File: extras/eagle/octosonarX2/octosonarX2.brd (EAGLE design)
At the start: 68.6 x 45.7 mm, 47 parts, among them IC1 74HC125D, IC2 74HC125D, IC3 74HC125D, IC4 74HC125D, IC5 PCF8575C

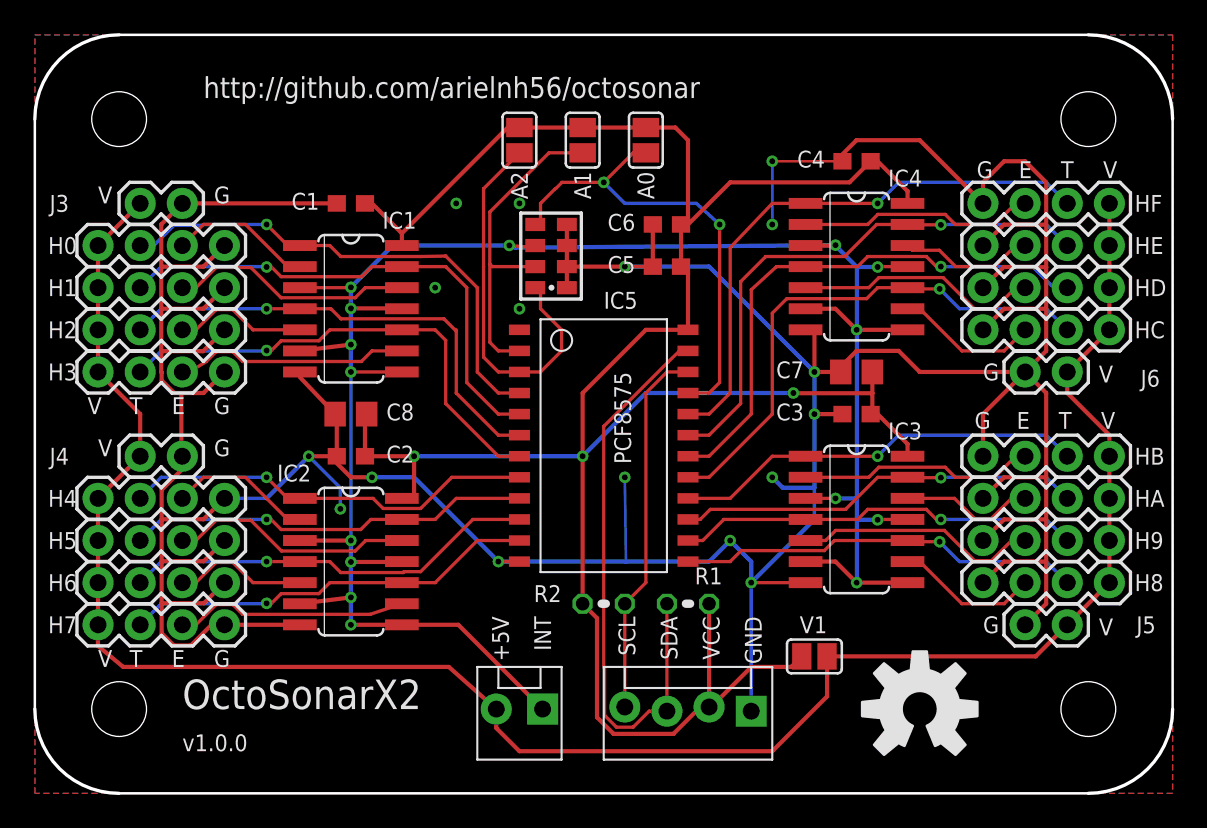
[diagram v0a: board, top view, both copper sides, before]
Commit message: Update octosonarX2.brd to 1.0.1
Moved the 5V line away from the screw hole by moving it to bottom layer. This never caused any reported problem, but I was worried about it and was supplying a plastic screw with each unit just in case. This error was introduced between v0 and V1 when I re-did all the power lines at 10mil.
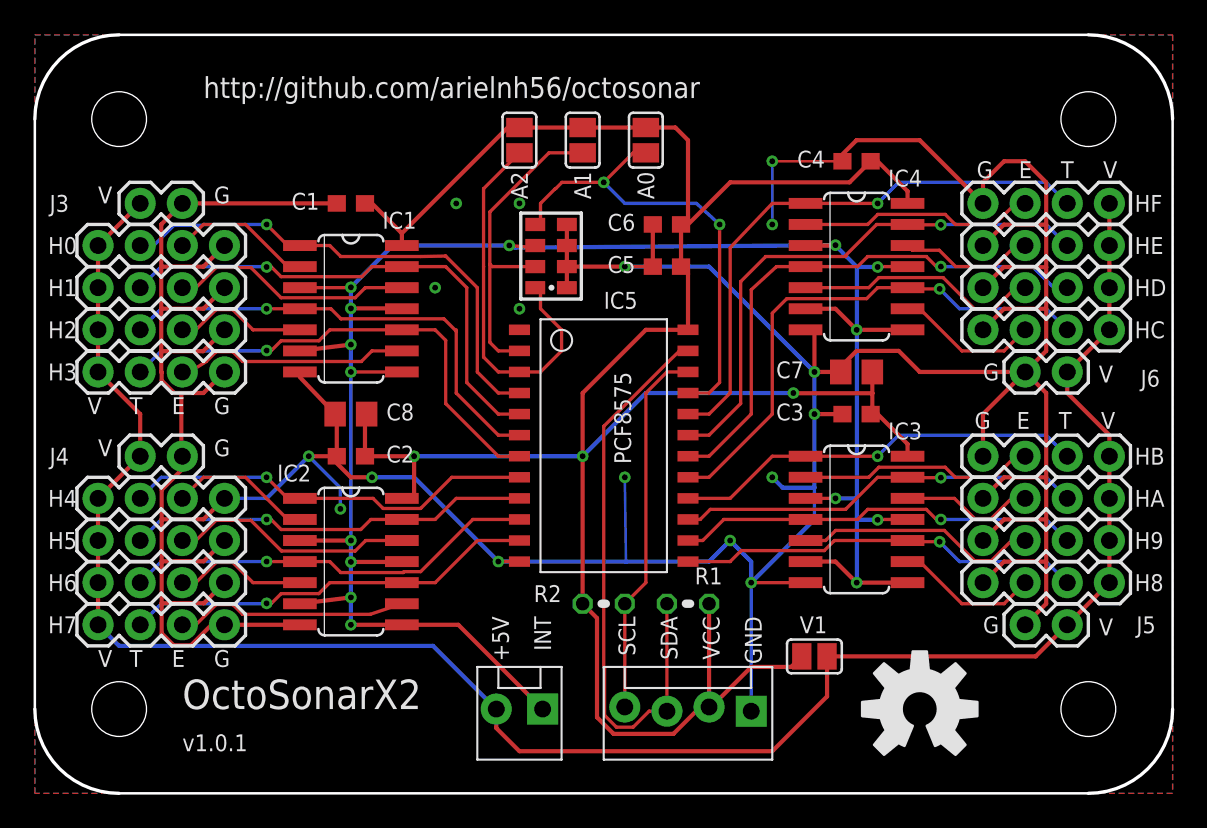
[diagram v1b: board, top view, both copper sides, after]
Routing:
- net +5V: track 124.7 -> 123.9 mm
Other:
- board text added: "v1.0.1"
- board text removed: "v1.0.0"
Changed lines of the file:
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@@
 <?xml version="1.0" encoding="utf-8"?>
 <!DOCTYPE eagle SYSTEM "eagle.dtd">
-<eagle version="8.2.2">
+<eagle version="9.2.2">
 <drawing>
 <settings>
 <setting alwaysvectorfont="no"/>
+<setting keepoldvectorfont="yes"/>
 <setting verticaltext="up"/>
 </settings>
@@
 <layer number="21" name="tPlace" color="7" fill="1" visible="yes" active="yes"/>
 <layer number="22" name="bPlace" color="7" fill="1" visible="no" active="yes"/>
-<layer number="23" name="tOrigins" color="15" fill="1" visible="no" active="yes"/>
+<layer number="23" name="tOrigins" color="15" fill="1" visible="yes" active="yes"/>
 <layer number="24" name="bOrigins" color="15" fill="1" visible="no" active="yes"/>
 <layer number="25" name="tNames" color="7" fill="1" visible="yes" active="yes"/>
@@
 <layer number="37" name="tTest" color="7" fill="1" visible="no" active="yes"/>
 <layer number="38" name="bTest" color="7" fill="1" visible="no" active="yes"/>
-<layer number="39" name="tKeepout" color="4" fill="11" visible="no" active="yes"/>
+<layer number="39" name="tKeepout" color="4" fill="11" visible="yes" active="yes"/>
 <layer number="40" name="bKeepout" color="1" fill="11" visible="no" active="yes"/>
-<layer number="41" name="tRestrict" color="4" fill="10" visible="no" active="yes"/>
+<layer number="41" name="tRestrict" color="4" fill="10" visible="yes" active="yes"/>
 <layer number="42" name="bRestrict" color="1" fill="10" visible="no" active="yes"/>
 <layer number="43" name="vRestrict" color="2" fill="10" visible="no" active="yes"/>
@@
 <layer number="49" name="Reference" color="7" fill="1" visible="no" active="yes"/>
 <layer number="50" name="dxf" color="7" fill="1" visible="no" active="no"/>
-<layer number="51" name="tDocu" color="7" fill="1" visible="no" active="yes"/>
+<layer number="51" name="tDocu" color="7" fill="1" visible="yes" active="yes"/>
 <layer number="52" name="bDocu" color="7" fill="1" visible="no" active="yes"/>
 <layer number="53" name="tGND_GNDA" color="7" fill="9" visible="no" active="no"/>
@@
 <text x="8.89" y="5.08" size="1.778" layer="21" font="vector" ratio="15">OctoSonarX2</text>
 <text x="10.16" y="41.91" size="1.27" layer="21" font="vector" ratio="15">http://github.com/arielnh56/octosonar</text>
-<text x="8.89" y="2.54" size="1.016" layer="21" font="vector" ratio="15">v1.0.0</text>
+<text x="8.89" y="2.54" size="1.016" layer="21" font="vector" ratio="15">v1.0.1</text>
 <text x="64.389" y="37.084" size="1.016" layer="21" font="vector" ratio="15">V</text>
 <text x="3.81" y="20.32" size="1.016" layer="21" font="vector" ratio="15">V</text>
@@
 <param name="dpMaxLengthDifference" value="10mm"/>
 <param name="dpGapFactor" value="2.5"/>
-<param name="checkGrid" value="0"/>
 <param name="checkAngle" value="0"/>
 <param name="checkFont" value="1"/>
 <param name="checkRestrict" value="1"/>
+<param name="checkStop" value="0"/>
+<param name="checkValues" value="0"/>
+<param name="checkNames" value="1"/>
+<param name="checkWireStubs" value="1"/>
+<param name="checkPolygonWidth" value="0"/>
 <param name="useDiameter" value="13"/>
 <param name="maxErrors" value="50"/>
@@
 <attribute name="VALUE" x="63.5" y="27.432" size="0.6096" layer="27" font="vector" ratio="20" rot="R180"/>
 </element>
-<element name="LOGO1" library="SparkFun-Aesthetics" package="OSHW-LOGO-L" value="OSHW-LOGOL" x="53.34" y="5.08"/>
+<element name="LOGO1" library="SparkFun-Aesthetics" package="OSHW-LOGO-L" value="OSHW-LOGOL" x="53.34" y="5.08" smashed="yes"/>
 </elements>
 <signals>
@@
 <contactref element="J5" pad="1"/>
 <contactref element="J4" pad="1"/>
-<wire x1="3.801575" y1="8.89" x2="3.81" y2="10.16" width="0.254" layer="1"/>
-<wire x1="5.325575" y1="7.62" x2="3.801575" y2="8.89" width="0.254" layer="1"/>
 <wire x1="3.81" y1="10.16" x2="3.81" y2="12.7" width="0.254" layer="1"/>
 <wire x1="3.81" y1="12.7" x2="3.81" y2="15.24" width="0.254" layer="1"/>
@@
 <wire x1="64.77" y1="30.48" x2="64.77" y2="33.02" width="0.254" layer="1"/>
 <wire x1="64.77" y1="33.02" x2="64.77" y2="35.56" width="0.254" layer="1"/>
-<wire x1="24.952628125" y1="7.62" x2="27.813" y2="5.08" width="0.254" layer="1"/>
-<wire x1="24.952628125" y1="7.62" x2="5.325575" y2="7.62" width="0.254" layer="1"/>
 <wire x1="62.23" y1="10.16" x2="60.325" y2="8.255" width="0.254" layer="1"/>
 <wire x1="60.325" y1="8.255" x2="47.752" y2="8.255" width="0.254" layer="1"/>
@@
 <wire x1="47.752" y1="5.842" x2="44.45" y2="2.54" width="0.254" layer="1"/>
 <wire x1="62.23" y1="24.13" x2="64.77" y2="21.59" width="0.254" layer="1"/>
-<wire x1="64.77" y1="21.59" x2="64.77" y2="20.13846875" width="0.254" layer="1"/>
+<wire x1="64.77" y1="21.59" x2="64.77" y2="20.32" width="0.254" layer="1"/>
+<wire x1="27.813" y1="5.08" x2="24.003" y2="8.89" width="0.254" layer="16"/>
+<wire x1="5.08" y1="8.89" x2="3.81" y2="10.16" width="0.254" layer="16"/>
+<wire x1="24.003" y1="8.89" x2="5.08" y2="8.89" width="0.254" layer="16"/>
 </signal>
 <signal name="N$23">
@@
 </signal>
 </signals>
+<mfgpreviewcolors>
+<mfgpreviewcolor name="soldermaskcolor" color="0xC8008000"/>
+<mfgpreviewcolor name="silkscreencolor" color="0xFFFEFEFE"/>
+<mfgpreviewcolor name="backgroundcolor" color="0xFF282828"/>
+<mfgpreviewcolor name="coppercolor" color="0xFFFFBF00"/>
+<mfgpreviewcolor name="substratecolor" color="0xFF786E46"/>
+</mfgpreviewcolors>
 <errors>
 </errors>
@@
 <compatibility>
 <note version="8.2" severity="warning">
-Since Version 8.2, Eagle supports online libraries. The ids
+Since Version 8.2, EAGLE supports online libraries. The ids
 of those online libraries will not be understood (or retained)
 with this version.
